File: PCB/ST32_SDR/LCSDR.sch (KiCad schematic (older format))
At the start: 6 parts, among them J10 Conn_01x01, J11 Conn_01x01, J6 IQ, J7 CLK, J8 Conn_01x01, J9 Conn_01x01

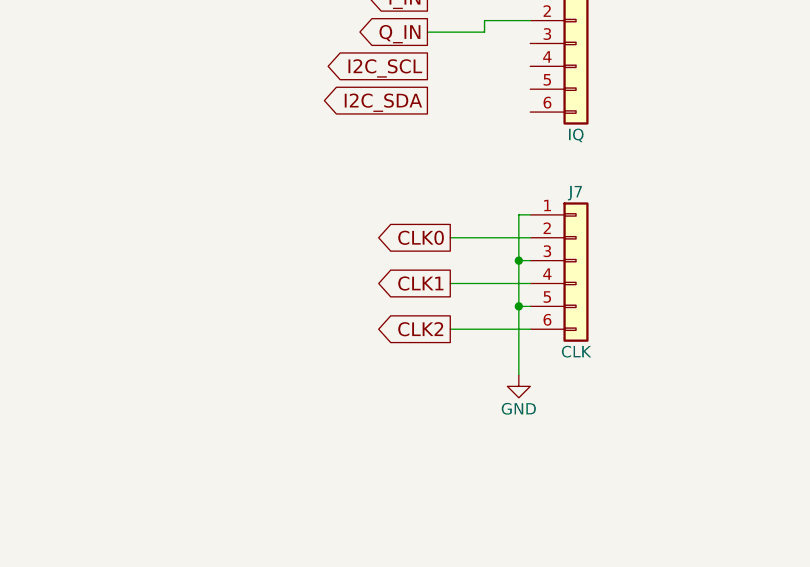
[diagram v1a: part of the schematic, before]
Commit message: PCB Linux 2, update AUDIO_OUT
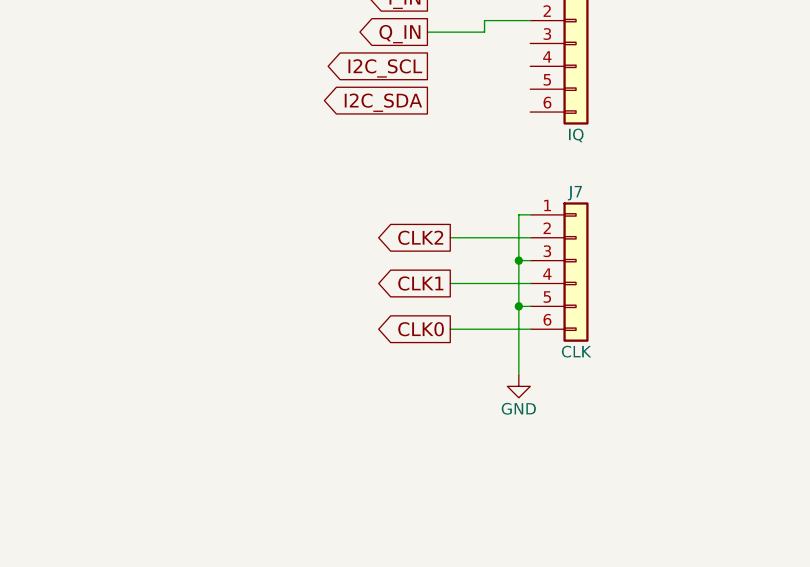
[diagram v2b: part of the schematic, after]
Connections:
- net CLK0: now also J7.6 (Pin_6); no longer J7.2 (Pin_2)
- net CLK2: now also J7.2 (Pin_2); no longer J7.6 (Pin_6)
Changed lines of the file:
@@
 LIBS:4ms-ic
 LIBS:Display
-LIBS:switches
-LIBS:cmos4000
+LIBS:Connector
+LIBS:Relay
 LIBS:LCSDR-cache
 EELAYER 25 0
@@
 	1    0    0    -1
 $EndComp
-Text GLabel 9150 2150 0    60   Output ~ 0
+Text GLabel 9150 2550 0    60   Output ~ 0
 CLK0
 Text GLabel 9150 2350 0    60   Output ~ 0
 CLK1
-Text GLabel 9150 2550 0    60   Output ~ 0
+Text GLabel 9150 2150 0    60   Output ~ 0
 CLK2
 Wire Wire Line
